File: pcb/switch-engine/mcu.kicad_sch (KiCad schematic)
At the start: 78 parts, among them J10 CORTEX_DEBUG_ETM, J12 CONN_01X03, J13 PMOD_HOST, J26 RJ45, J9 PMOD_HOST, U14 ECS-1612MV-250-CN, U17 AT24MAC402, U29 ADM3101E_QFN, U8 XCKU5P-2FFVB676I, U9 STM32H735-UFBGA176-25

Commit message: More progress on PHY layout
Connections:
- net FMC_A20: now also U8.G12 (IO_L5P_HDGC_87); no longer U8.J15 (IO_L4P_AD12P_87)
- net FMC_A22: now also U8.J15 (IO_L4P_AD12P_87); no longer U8.G12 (IO_L5P_HDGC_87)
- net FMC_A25: now also U8.F13 (IO_L6N_HDGC_87); no longer U8.F14 (IO_L6P_HDGC_87)
- net FMC_AD2: now also U8.D13 (IO_L8N_HDGC_87); no longer U8.F13 (IO_L6N_HDGC_87)
- net FMC_NL_NADV: now also U8.F14 (IO_L6P_HDGC_87); no longer U8.D13 (IO_L8N_HDGC_87)
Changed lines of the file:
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@@
 	)
 	(label "FMC_A25"
-		(at 294.64 52.07 180)
+		(at 294.64 49.53 180)
 		(fields_autoplaced yes)
 		(effects
@@
 	)
 	(label "FMC_A20"
-		(at 294.64 62.23 180)
+		(at 294.64 57.15 180)
 		(fields_autoplaced yes)
 		(effects
@@
 	)
 	(label "FMC_AD2"
-		(at 294.64 49.53 180)
+		(at 294.64 39.37 180)
 		(fields_autoplaced yes)
 		(effects
@@
 	)
 	(label "FMC_A22"
-		(at 294.64 57.15 180)
+		(at 294.64 62.23 180)
 		(fields_autoplaced yes)
 		(effects
@@
 	)
 	(label "FMC_NL_NADV"
-		(at 294.64 39.37 180)
-		(fields_autoplaced yes)
-		(effects
+		(at 294.64 52.07 180)
+		(fields_autoplaced yes)
+		(effects

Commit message: Routing cleanup around FMC, still needs a lot more
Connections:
- net FAN1_PWM: now also U9.P11 (PF12); no longer U9.R2 (PA2)
- net FAN1_TACH: now also U9.P15 (PH6); no longer U9.P1 (PA0)
- net FAN2_PWM: now also U9.N11 (PF13); no longer U9.N5 (PA3)
- net FAN2_TACH: now also U9.M14 (PH9); no longer U9.P2 (PA1)
- net FMC_A23: now also U8.G10 (IO_L5P_HDGC_AD7P_86); no longer U8.F10 (IO_L6P_HDGC_AD6P_86)
- net FMC_NBL1: now also U8.F10 (IO_L6P_HDGC_AD6P_86); no longer U8.G10 (IO_L5P_HDGC_AD7P_86)
- net SFP0_SCL: now also U9.M13 (PH11); no longer U9.A2 (PB8)
- net SFP0_SDA: now also U9.N15 (PH12); no longer U9.B3 (PB9)

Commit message: Lots of routing cleanup around MCU
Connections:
- net FMC_A16: now also U8.B14 (IO_L12P_AD8P_87); no longer U8.C9 (IO_L9N_AD3N_86)
- net FMC_A17: now also U8.A14 (IO_L12N_AD8N_87); no longer U8.D9 (IO_L9P_AD3P_86)
- net FMC_A18: now also U8.C14 (IO_L9P_AD11P_87); no longer U8.E10 (IO_L7N_HDGC_AD5N_86)
- net FMC_A19: now also U8.K10 (IO_L1P_AD11P_86); no longer U8.G11 (IO_L4N_AD8N_86)
- net FMC_A20: now also U8.J11 (IO_L2P_AD10P_86); no longer U8.G12 (IO_L5P_HDGC_87)
- net FMC_A21: now also U8.F10 (IO_L6P_HDGC_AD6P_86); no longer U8.G14 (IO_L3N_AD13N_87)
- net FMC_A22: now also U8.G9 (IO_L5N_HDGC_AD7N_86); no longer U8.J15 (IO_L4P_AD12P_87)
- net FMC_A24: now also U8.D11 (IO_L8P_HDGC_AD4P_86); no longer U8.E12 (IO_L7N_HDGC_87)
- net FMC_A25: now also U8.E11 (IO_L7P_HDGC_AD5P_86); no longer U8.F13 (IO_L6N_HDGC_87)
- net FMC_AD0: now also U8.D13 (IO_L8N_HDGC_87); no longer U8.D10 (IO_L8N_HDGC_AD4N_86)
- net FMC_AD1: now also U8.E12 (IO_L7N_HDGC_87); no longer U8.C11 (IO_L12P_AD0P_86)
- net FMC_AD10: now also U8.A13 (IO_L11P_AD9P_87); no longer U8.A14 (IO_L12N_AD8N_87)
- net FMC_AD11: now also U8.D10 (IO_L8N_HDGC_AD4N_86); no longer U8.C12 (IO_L10P_AD10P_87)
- net FMC_AD12: now also U8.A12 (IO_L11N_AD9N_87); no longer U8.B12 (IO_L10N_AD10N_87)
- net FMC_AD13: now also U8.B12 (IO_L10N_AD10N_87); no longer U8.A13 (IO_L11P_AD9P_87)
- net FMC_AD14: now also U8.C13 (IO_L9N_AD11N_87); no longer U8.B14 (IO_L12P_AD8P_87)
- net FMC_AD15: now also U8.E10 (IO_L7N_HDGC_AD5N_86); no longer U8.C14 (IO_L9P_AD11P_87)
- net FMC_AD2: now also U8.C12 (IO_L10P_AD10P_87); no longer U8.D13 (IO_L8N_HDGC_87)
- net FMC_AD3: now also U8.G11 (IO_L4N_AD8N_86); no longer U8.G9 (IO_L5N_HDGC_AD7N_86)
- net FMC_AD8: now also U8.C11 (IO_L12P_AD0P_86); no longer U8.A12 (IO_L11N_AD9N_87)
- net FMC_NBL1: now also U8.H11 (IO_L4P_AD8P_86); no longer U8.F10 (IO_L6P_HDGC_AD6P_86)
- net FMC_NE1: now also U8.F14 (IO_L6P_HDGC_87); no longer U8.C13 (IO_L9N_AD11N_87)
- net FMC_NE2: now also U8.D9 (IO_L9P_AD3P_86); no longer U8.F12 (IO_L5N_HDGC_87)
- net FMC_NE3: now also U8.E13 (IO_L7P_HDGC_87); no longer U8.D11 (IO_L8P_HDGC_AD4P_86)
- net FMC_NL_NADV: now also U8.G14 (IO_L3N_AD13N_87); no longer U8.F14 (IO_L6P_HDGC_87)
- net FMC_NWAIT: now also U8.F13 (IO_L6N_HDGC_87); no longer U8.E13 (IO_L7P_HDGC_87)
- net FMC_NWE: now also U8.C9 (IO_L9N_AD3N_86); no longer U8.E11 (IO_L7P_HDGC_AD5P_86)
- net FPGA_PMOD_DQ0: now also U8.F12 (IO_L5N_HDGC_87); no longer U8.K10 (IO_L1P_AD11P_86)
- net FPGA_PMOD_DQ1: now also U8.H12 (IO_L1N_AD15N_87); no longer U8.J11 (IO_L2P_AD10P_86)
- net FPGA_PMOD_DQ2: now also U8.H13 (IO_L2N_AD14N_87); no longer U8.J12 (IO_L1P_AD15P_87)
- net FPGA_PMOD_DQ3: now also U8.J14 (IO_L4N_AD12N_87); no longer U8.J13 (IO_L2P_AD14P_87)
- net FPGA_PMOD_DQ4: now also U8.G12 (IO_L5P_HDGC_87); no longer U8.H11 (IO_L4P_AD8P_86)
- net FPGA_PMOD_DQ5: now also U8.J12 (IO_L1P_AD15P_87); no longer U8.H12 (IO_L1N_AD15N_87)
- net FPGA_PMOD_DQ6: now also U8.J13 (IO_L2P_AD14P_87); no longer U8.H13 (IO_L2N_AD14N_87)
- net FPGA_PMOD_DQ7: now also U8.J15 (IO_L4P_AD12P_87); no longer U8.J14 (IO_L4N_AD12N_87)
- net MCU_READY: now also U9.N14 (PH10); no longer U9.H3 (PF5)
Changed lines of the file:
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@@
 	)
 	(no_connect
+		(at 83.82 88.9)
+	)
+	(no_connect
 		(at 179.07 106.68)
 	)
@@
 	)
 	(no_connect
-		(at 127 101.6)
-	)
-	(no_connect
 		(at 83.82 114.3)
 	)
@@
 	)
 	(label "FPGA_PMOD_DQ6"
-		(at 294.64 69.85 180)
+		(at 294.64 72.39 180)
 		(fields_autoplaced yes)
 		(effects
@@
 	)
 	(label "FMC_AD3"
-		(at 228.6 54.61 180)
+		(at 228.6 59.69 180)
 		(fields_autoplaced yes)
 		(effects
@@
 	)
 	(label "FMC_NWE"
-		(at 228.6 46.99 180)
+		(at 228.6 34.29 180)
 		(fields_autoplaced yes)
 		(effects
@@
 	)
 	(label "FMC_A25"
-		(at 294.64 49.53 180)
+		(at 228.6 46.99 180)
 		(fields_autoplaced yes)
 		(effects
@@
 	)
 	(label "FMC_A18"
-		(at 228.6 44.45 180)
+		(at 294.64 36.83 180)
 		(fields_autoplaced yes)
 		(effects
@@
 	)
 	(label "FMC_NE3"
-		(at 228.6 41.91 180)
+		(at 294.64 46.99 180)
 		(fields_autoplaced yes)
 		(effects
@@
 	)
 	(label "FMC_NBL1"
-		(at 228.6 52.07 180)
+		(at 228.6 62.23 180)
 		(fields_autoplaced yes)
 		(effects
@@
 	)
 	(label "FPGA_PMOD_DQ4"
-		(at 228.6 62.23 180)
+		(at 294.64 57.15 180)
 		(fields_autoplaced yes)
 		(effects
@@
 	)
 	(label "FMC_AD11"
-		(at 294.64 31.75 180)
+		(at 228.6 39.37 180)
 		(fields_autoplaced yes)
 		(effects
@@
 	)
 	(label "FMC_NWAIT"
-		(at 294.64 46.99 180)
+		(at 294.64 49.53 180)
 		(fields_autoplaced yes)
 		(effects
@@
 	)
 	(label "FMC_AD1"
-		(at 228.6 21.59 180)
+		(at 294.64 44.45 180)
 		(fields_autoplaced yes)
 		(effects
@@
 	)
 	(label "FMC_A21"
-		(at 294.64 64.77 180)
+		(at 228.6 52.07 180)
 		(fields_autoplaced yes)
 		(effects
@@
 	)
 	(label "FMC_AD14"
-		(at 294.64 21.59 180)
+		(at 294.64 34.29 180)
 		(fields_autoplaced yes)
 		(effects
@@
 	)
 	(label "FMC_A20"
-		(at 294.64 57.15 180)
+		(at 228.6 72.39 180)
 		(fields_autoplaced yes)
 		(effects
@@
 	)
 	(label "FPGA_PMOD_DQ5"
-		(at 294.64 74.93 180)
+		(at 294.64 77.47 180)
 		(fields_autoplaced yes)
 		(effects
@@
 	)
 	(label "FPGA_PMOD_DQ7"
-		(at 294.64 59.69 180)
+		(at 294.64 62.23 180)
 		(fields_autoplaced yes)
 		(effects
@@
 	)
 	(label "FMC_AD10"
-		(at 294.64 19.05 180)
+		(at 294.64 26.67 180)
 		(fields_autoplaced yes)
 		(effects
@@
 	)
 	(label "FPGA_PMOD_DQ3"
-		(at 294.64 72.39 180)
+		(at 294.64 59.69 180)
 		(fields_autoplaced yes)
 		(effects
@@
 	)
 	(label "FMC_AD2"
-		(at 294.64 39.37 180)
+		(at 294.64 31.75 180)
 		(fields_autoplaced yes)
 		(effects
@@
 	)
 	(label "FPGA_PMOD_DQ0"
-		(at 228.6 77.47 180)
+		(at 294.64 54.61 180)
 		(fields_autoplaced yes)
 		(effects
@@
 	)
 	(label "FMC_A22"
-		(at 294.64 62.23 180)
+		(at 228.6 54.61 180)
 		(fields_autoplaced yes)
 		(effects
@@
 	)
 	(label "FMC_A24"
-		(at 294.64 44.45 180)
+		(at 228.6 41.91 180)
 		(fields_autoplaced yes)
 		(effects
@@
 	)
 	(label "FMC_NL_NADV"
-		(at 294.64 52.07 180)
+		(at 294.64 64.77 180)
 		(fields_autoplaced yes)
 		(effects
@@
 	)
 	(label "FPGA_PMOD_DQ2"
-		(at 294.64 77.47 180)
+		(at 294.64 69.85 180)
 		(fields_autoplaced yes)
 		(effects
@@
 	)
 	(label "FMC_AD13"
-		(at 294.64 26.67 180)
+		(at 294.64 29.21 180)
 		(fields_autoplaced yes)
 		(effects
@@
 	)
 	(label "FMC_A17"
-		(at 228.6 36.83 180)
+		(at 294.64 19.05 180)
 		(fields_autoplaced yes)
 		(effects
@@
 	)
 	(label "FPGA_PMOD_DQ1"
-		(at 228.6 72.39 180)
+		(at 294.64 74.93 180)
 		(fields_autoplaced yes)
 		(effects
@@
 	)
 	(label "FMC_AD15"
-		(at 294.64 36.83 180)
+		(at 228.6 44.45 180)
 		(fields_autoplaced yes)
 		(effects
@@
 	)
 	(label "FMC_AD8"
-		(at 294.64 24.13 180)
+		(at 228.6 21.59 180)
 		(fields_autoplaced yes)
 		(effects
@@
 	)
 	(label "FMC_NE1"
-		(at 294.64 34.29 180)
+		(at 294.64 52.07 180)
 		(fields_autoplaced yes)
 		(effects
@@
 	)
 	(label "FMC_AD0"
-		(at 228.6 39.37 180)
+		(at 294.64 39.37 180)
 		(fields_autoplaced yes)
 		(effects
@@
 	)
 	(label "FMC_AD12"
-		(at 294.64 29.21 180)
+		(at 294.64 24.13 180)
 		(fields_autoplaced yes)
 		(effects
@@
 	)
 	(label "FMC_A19"
-		(at 228.6 59.69 180)
+		(at 228.6 77.47 180)
 		(fields_autoplaced yes)
 		(effects
@@
 	)
 	(label "FMC_A16"
-		(at 228.6 34.29 180)
+		(at 294.64 21.59 180)
 		(fields_autoplaced yes)
 		(effects
@@
 	)
 	(label "FMC_NE2"
-		(at 294.64 54.61 180)
+		(at 228.6 36.83 180)
 		(fields_autoplaced yes)
 		(effects
@@
 	(hierarchical_label "MCU_READY"
 		(shape output)
-		(at 83.82 88.9 180)
+		(at 127 101.6 180)
 		(fields_autoplaced yes)
 		(effects

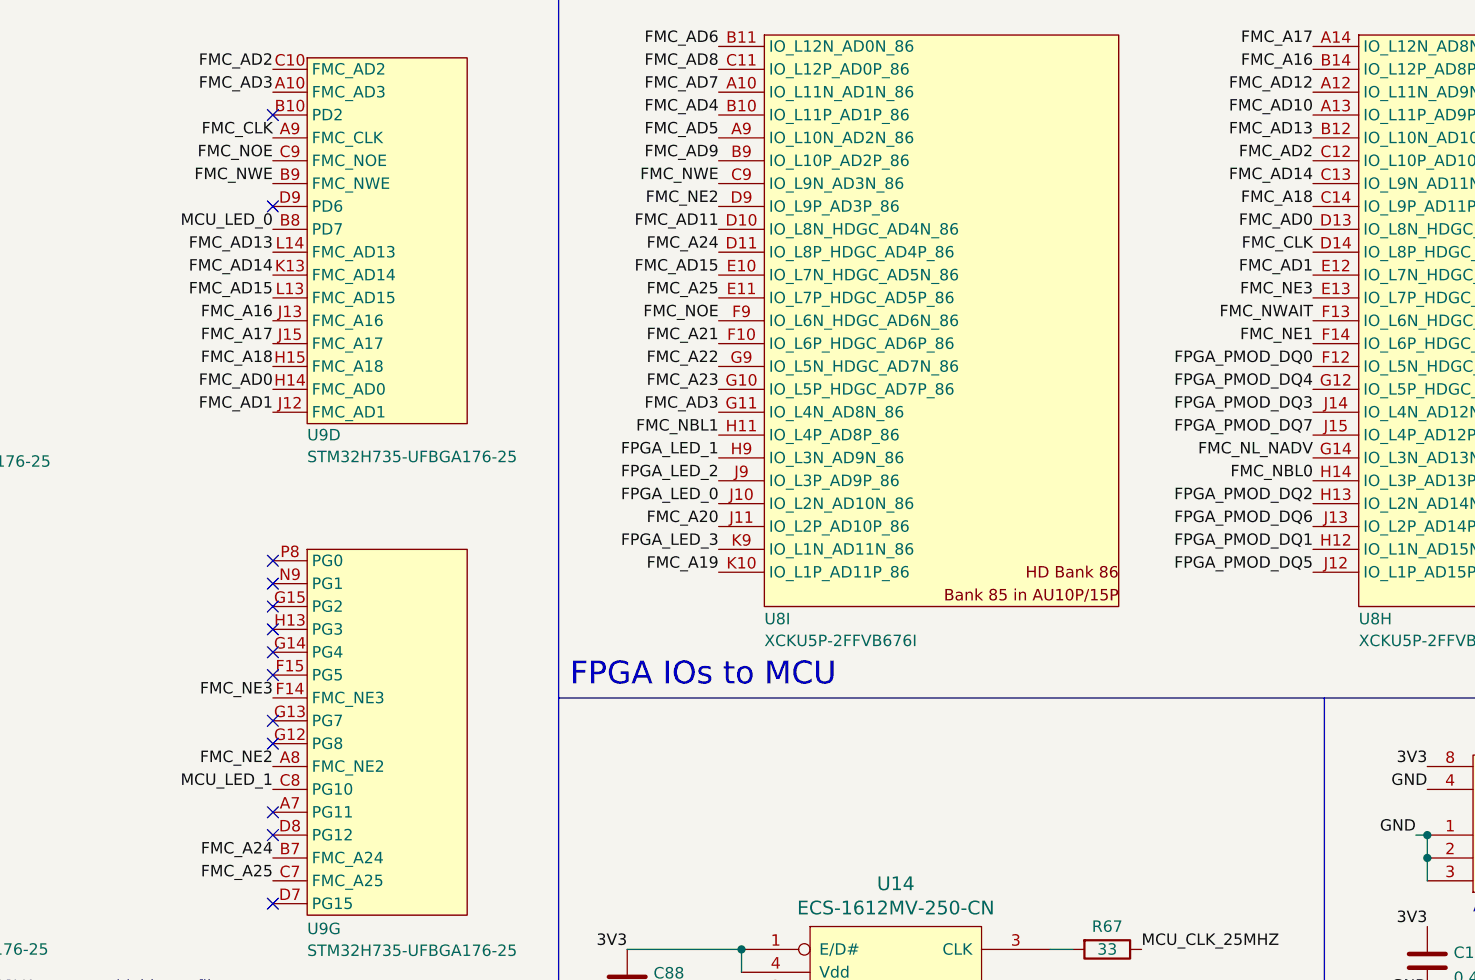
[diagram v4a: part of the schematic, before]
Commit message: Rerouted FMC to not need any mid-span vias
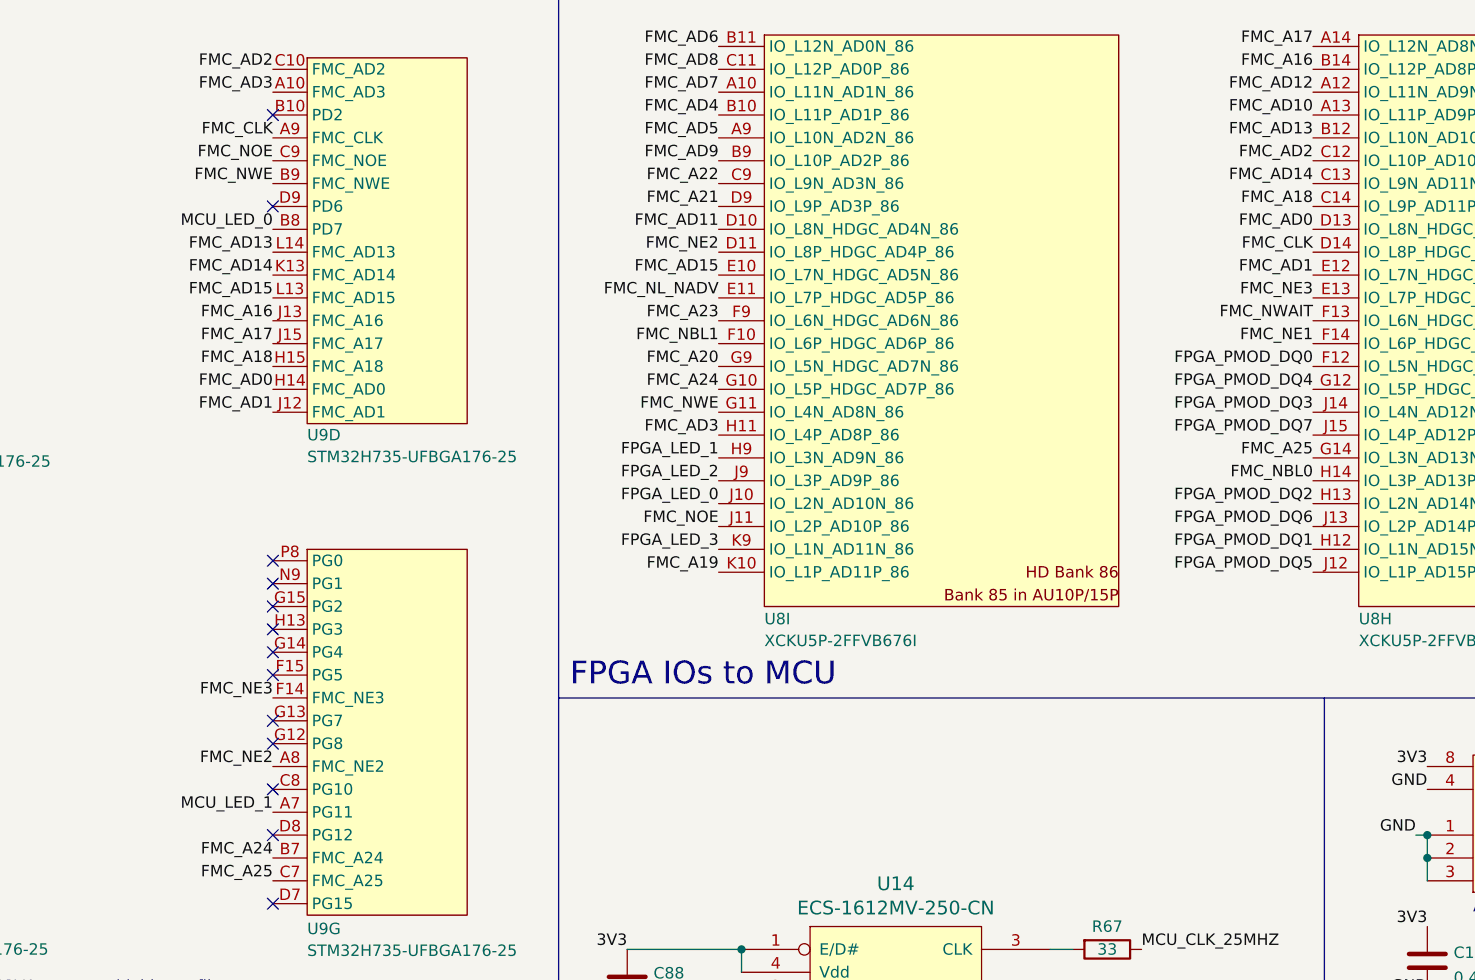
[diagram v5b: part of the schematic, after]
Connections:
- net FMC_A20: now also U8.G9 (IO_L5N_HDGC_AD7N_86); no longer U8.J11 (IO_L2P_AD10P_86)
- net FMC_A21: now also U8.D9 (IO_L9P_AD3P_86); no longer U8.F10 (IO_L6P_HDGC_AD6P_86)
- net FMC_A22: now also U8.C9 (IO_L9N_AD3N_86); no longer U8.G9 (IO_L5N_HDGC_AD7N_86)
- net FMC_A23: now also U8.F9 (IO_L6N_HDGC_AD6N_86); no longer U8.G10 (IO_L5P_HDGC_AD7P_86)
- net FMC_A24: now also U8.G10 (IO_L5P_HDGC_AD7P_86); no longer U8.D11 (IO_L8P_HDGC_AD4P_86)
- net FMC_A25: now also U8.G14 (IO_L3N_AD13N_87); no longer U8.E11 (IO_L7P_HDGC_AD5P_86)
- net FMC_AD3: now also U8.H11 (IO_L4P_AD8P_86); no longer U8.G11 (IO_L4N_AD8N_86)
- net FMC_NBL1: now also U8.F10 (IO_L6P_HDGC_AD6P_86); no longer U8.H11 (IO_L4P_AD8P_86)
- net FMC_NE2: now also U8.D11 (IO_L8P_HDGC_AD4P_86); no longer U8.D9 (IO_L9P_AD3P_86)
- net FMC_NL_NADV: now also U8.E11 (IO_L7P_HDGC_AD5P_86); no longer U8.G14 (IO_L3N_AD13N_87)
- net FMC_NOE: now also U8.J11 (IO_L2P_AD10P_86); no longer U8.F9 (IO_L6N_HDGC_AD6N_86)
- net FMC_NWE: now also U8.G11 (IO_L4N_AD8N_86); no longer U8.C9 (IO_L9N_AD3N_86)
- net MCU_LED_1: now also U9.A7 (PG11); no longer U9.C8 (PG10)
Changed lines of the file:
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@@
 	)
 	(no_connect
+		(at 179.07 101.6)
+	)
+	(no_connect
 		(at 127 52.07)
 	)
@@
 	)
 	(no_connect
-		(at 179.07 104.14)
-	)
-	(no_connect
 		(at 179.07 88.9)
 	)
@@
 	)
 	(label "FMC_AD3"
-		(at 228.6 59.69 180)
+		(at 228.6 62.23 180)
 		(fields_autoplaced yes)
 		(effects
@@
 	)
 	(label "FMC_NWE"
-		(at 228.6 34.29 180)
+		(at 228.6 59.69 180)
 		(fields_autoplaced yes)
 		(effects
@@
 	)
 	(label "FMC_A25"
-		(at 228.6 46.99 180)
+		(at 294.64 64.77 180)
 		(fields_autoplaced yes)
 		(effects
@@
 	)
 	(label "MCU_LED_1"
-		(at 179.07 101.6 180)
+		(at 179.07 104.14 180)
 		(fields_autoplaced yes)
 		(effects
@@
 	)
 	(label "FMC_NBL1"
-		(at 228.6 62.23 180)
+		(at 228.6 52.07 180)
 		(fields_autoplaced yes)
 		(effects
@@
 	)
 	(label "FMC_NOE"
-		(at 228.6 49.53 180)
+		(at 228.6 72.39 180)
 		(fields_autoplaced yes)
 		(effects
@@
 	)
 	(label "FMC_A21"
-		(at 228.6 52.07 180)
+		(at 228.6 36.83 180)
 		(fields_autoplaced yes)
 		(effects
@@
 	)
 	(label "FMC_A20"
-		(at 228.6 72.39 180)
+		(at 228.6 54.61 180)
 		(fields_autoplaced yes)
 		(effects
@@
 	)
 	(label "FMC_A23"
-		(at 228.6 57.15 180)
+		(at 228.6 49.53 180)
 		(fields_autoplaced yes)
 		(effects
@@
 	)
 	(label "FMC_A22"
-		(at 228.6 54.61 180)
+		(at 228.6 34.29 180)
 		(fields_autoplaced yes)
 		(effects
@@
 	)
 	(label "FMC_A24"
-		(at 228.6 41.91 180)
+		(at 228.6 57.15 180)
 		(fields_autoplaced yes)
 		(effects
@@
 	)
 	(label "FMC_NL_NADV"
-		(at 294.64 64.77 180)
+		(at 228.6 46.99 180)
 		(fields_autoplaced yes)
 		(effects
@@
 	)
 	(label "FMC_NE2"
-		(at 228.6 36.83 180)
+		(at 228.6 41.91 180)
 		(fields_autoplaced yes)
 		(effects
